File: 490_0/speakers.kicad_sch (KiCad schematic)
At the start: 9 parts, among them J15 Conn_01x07, J16 Conn_01x10, J20 S2B-XH-A, U9 MAX98357A

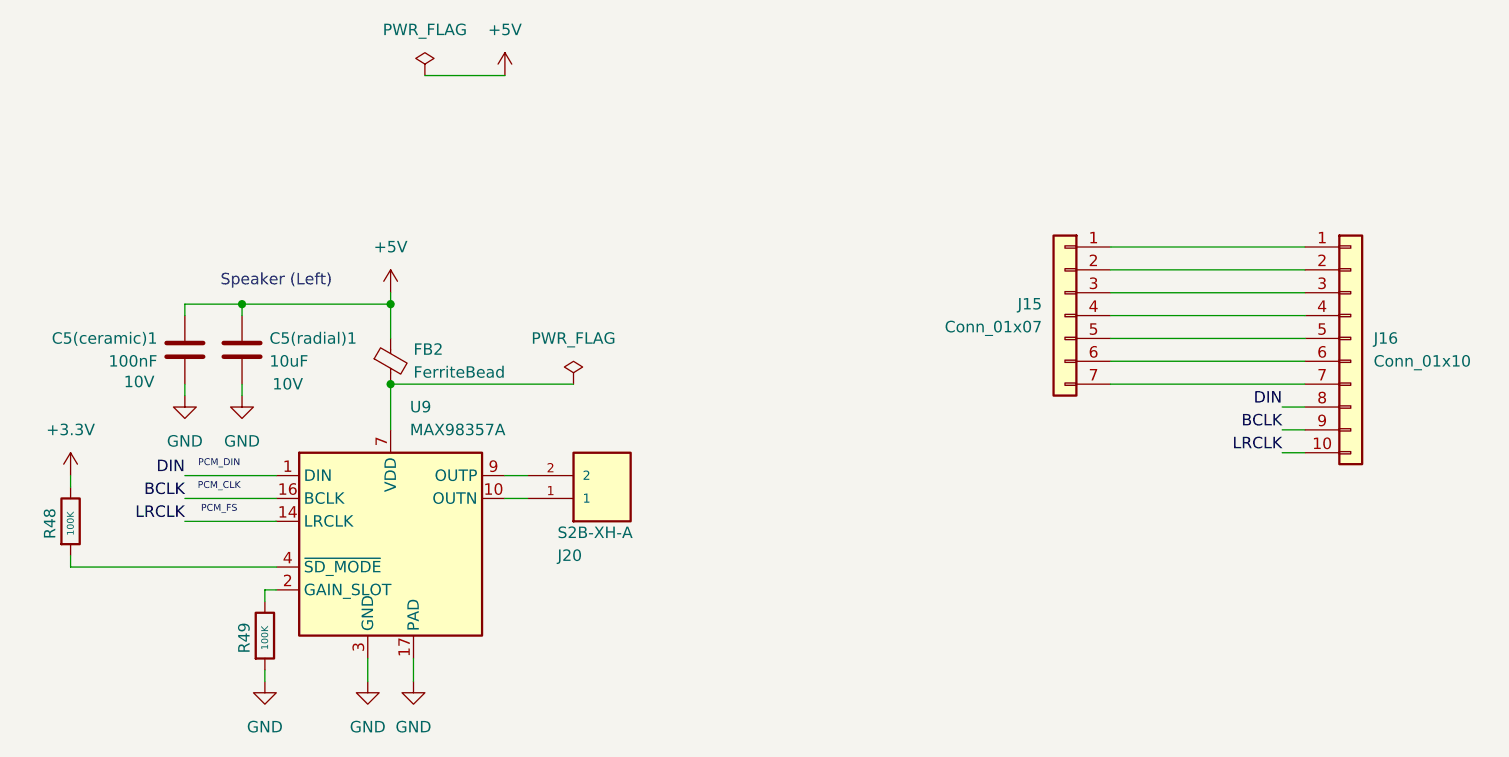
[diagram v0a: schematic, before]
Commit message: Schematic layout update
- applied hierarchical labels
- cleaned up the schematic
- finalized CM4 connections
- checked cm4 connections
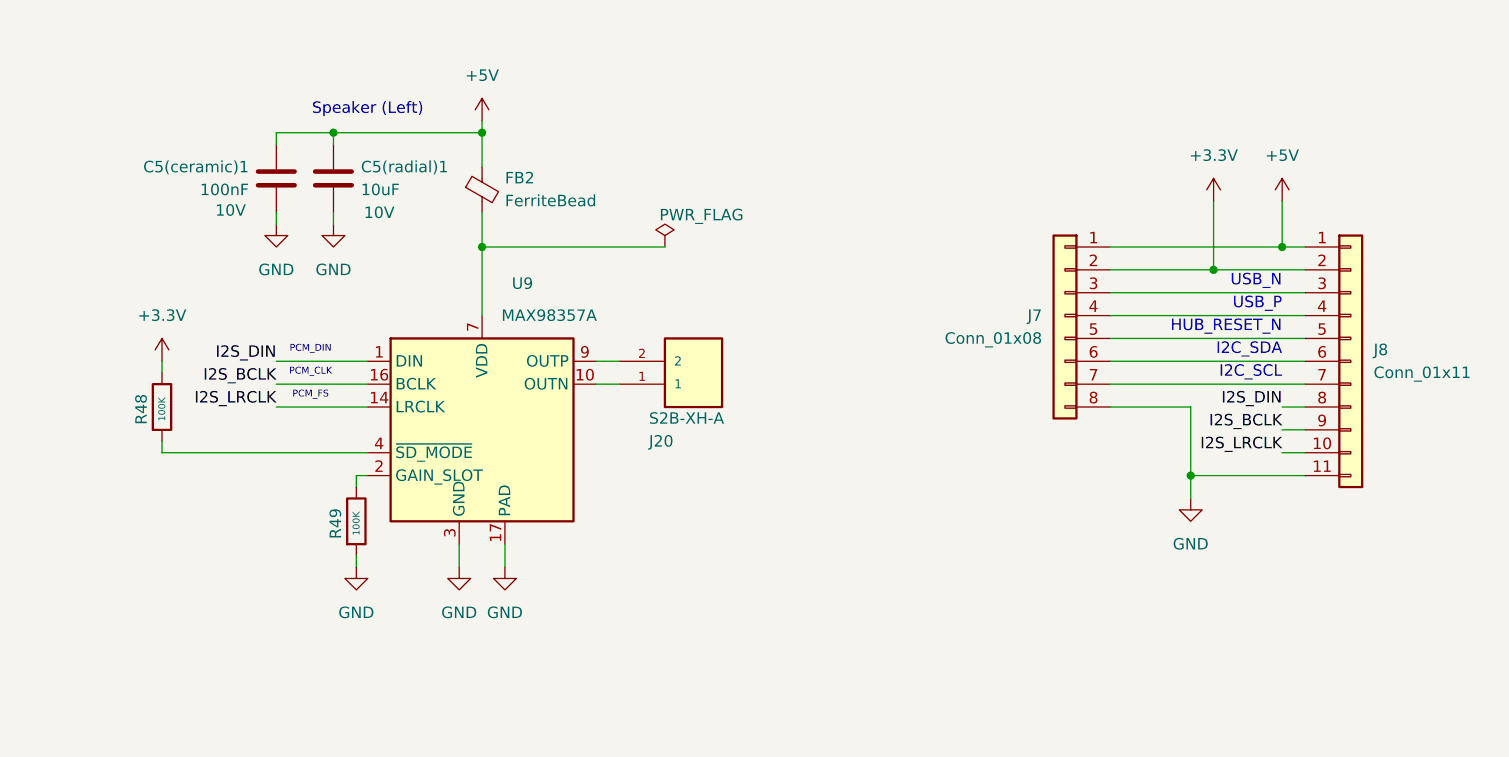
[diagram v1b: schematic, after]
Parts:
- removed J15: Conn_01x07, symbol Connector_Generic:Conn_01x07
- removed J16: Conn_01x10, symbol Connector_Generic:Conn_01x10
- added J7: Conn_01x08, 4ms_Connector:Pins_1x08_2.54mm_TH, symbol PCM_4ms_Connector:Conn_01x08
- added J8: Conn_01x11, symbol Connector_Generic:Conn_01x11
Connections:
- net +3.3V: now also J7.2 (Pin_2), J8.2 (Pin_2)
- net +5V: now also J7.1 (Pin_1), J8.1 (Pin_1)
- net GND: now also J7.8 (Pin_8), J8.11 (Pin_11)
- net BCLK renamed I2S_BCLK
- net I2S_BCLK: now also J8.9 (Pin_9)
- net DIN renamed I2S_DIN
- net I2S_DIN: now also J8.8 (Pin_8)
- net LRCLK renamed I2S_LRCLK
- net I2S_LRCLK: now also J8.10 (Pin_10)
- new net: J7.3 (Pin_3), J8.3 (Pin_3)
- new net: J7.4 (Pin_4), J8.4 (Pin_4)
- new net: J7.5 (Pin_5), J8.5 (Pin_5)
- new net: J7.6 (Pin_6), J8.6 (Pin_6)
- new net: J7.7 (Pin_7), J8.7 (Pin_7)
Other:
- note added: "HUB_RESET_N"
- note added: "I2C_SCL"
- note added: "I2C_SDA"
- note added: "USB_N"
- note added: "USB_P"
- moved on the sheet: C5(ceramic)1, C5(radial)1, FB2, J20, R48, R49, U9

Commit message: Power + BOM update
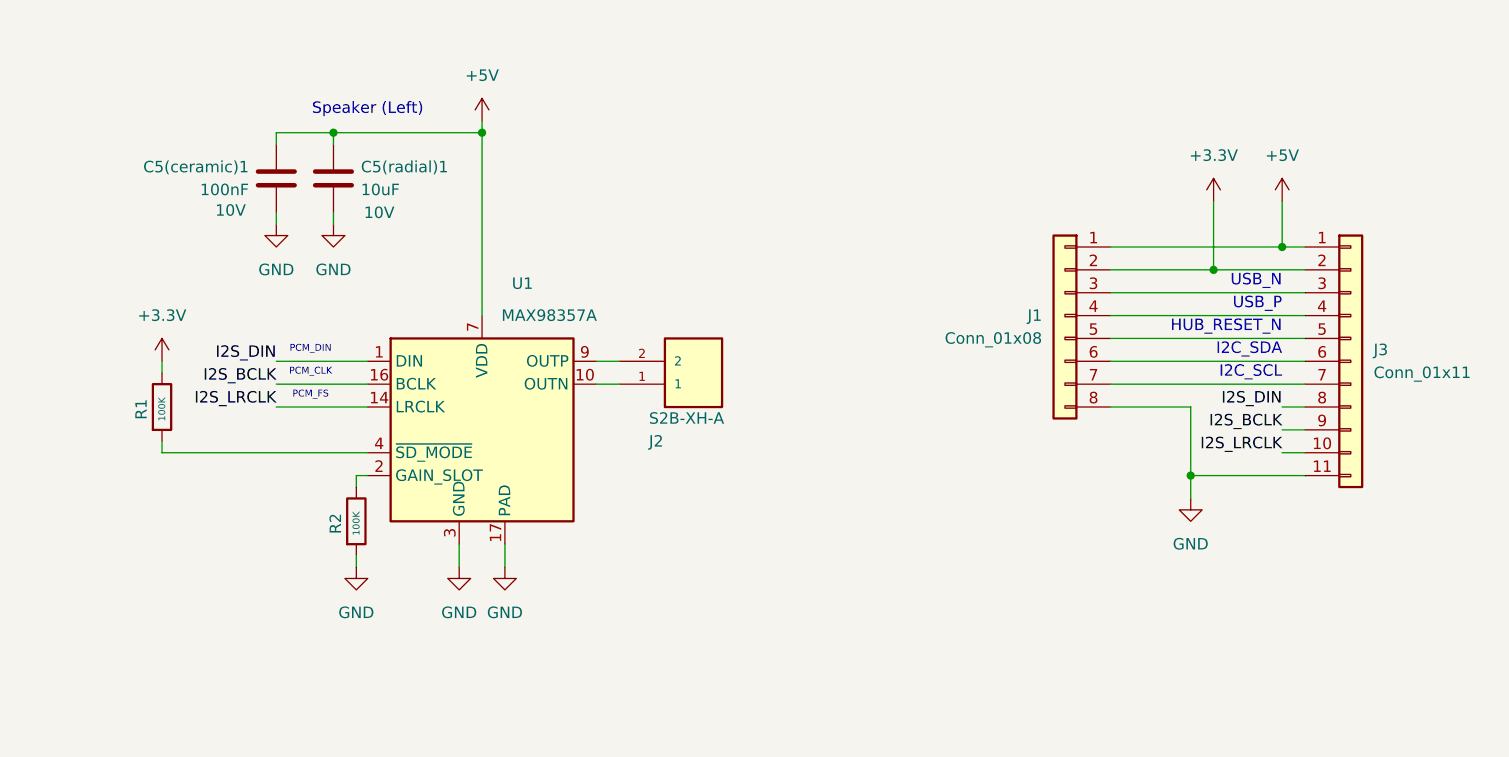
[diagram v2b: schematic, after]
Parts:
- removed FB2: FerriteBead, Capacitor_SMD:C_0603_1608Metric, symbol Device:FerriteBead_Small
- renumbered J7 to J1, J20 to J2, J8 to J3, R48 to R1, R49 to R2, U9 to U1
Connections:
- net +5V: now also U1.7 (VDD), U1.8 (VDD)

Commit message: finished BOM
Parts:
- removed C5(ceramic)1: 100nF, Capacitor_SMD:C_0603_1608Metric, symbol Device:C
- removed C5(radial)1: 10uF, Capacitor_THT:CP_Radial_D5.0mm_P2.50mm, symbol Device:C
- added C52: 100n, symbol Device:C
- added C53: 10u, symbol Device:C
- J1: footprint 4ms_Connector:Pins_1x08_2.54mm_TH -> (none); Digikey Link (none) -> https://www.digikey.ca/en/products/detail/jst-sales-america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; Manufacturer (none) -> JST Sales America Inc.; Manufacturer Part (none) -> S8B-XH-A; Price (none) -> 0.33; Supplier (none) -> DigiKey; Supplier P/N (none) -> 455-S8B-XH-A-ND; Type (none) -> Through Hole; Unit (none) -> pcs
- J3: Digikey Link (none) -> https://www.digikey.ca/en/products/detail/jst-sales-america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; Manufacturer (none) -> JST Sales America Inc.; Manufacturer Part (none) -> S11B-XH-A; Price (none) -> 0.47; Supplier (none) -> DigiKey; Supplier P/N (none) -> 455-S11B-XH-A-ND; Type (none) -> Through Hole; Unit (none) -> pcs
- R1, R2: Digikey Link (none) -> https://www.digikey.ca/en/products/detail/yageo/RC1206FR-07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; Manufacturer (none) -> YAGEO; Manufacturer Part (none) -> RC1206FR-07100KL; Package (none) -> 1206; Price (none) -> 0.1; Supplier (none) -> DigiKey; Supplier P/N (none) -> 311-100KFRCT-ND; Type (none) -> SMD; Unit (none) -> pcs
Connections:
- net +5V: now also C52.1, C53.1
- net GND: now also C52.2, C53.2
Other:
- note added: "10V"

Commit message: Updated the schematic
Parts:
- removed J1: Conn_01x08, symbol PCM_4ms_Connector:Conn_01x08
- removed J3: Conn_01x11, symbol Connector_Generic:Conn_01x11
- renumbered C52 to C35, C53 to C36, J2 to J25, R1 to R37, R2 to R38, U1 to U7
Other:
- note removed: "HUB_RESET_N"
- note removed: "I2C_SCL"
- note removed: "I2C_SDA"
- note removed: "USB_N"
- note removed: "USB_P"
- moved on the sheet: R37

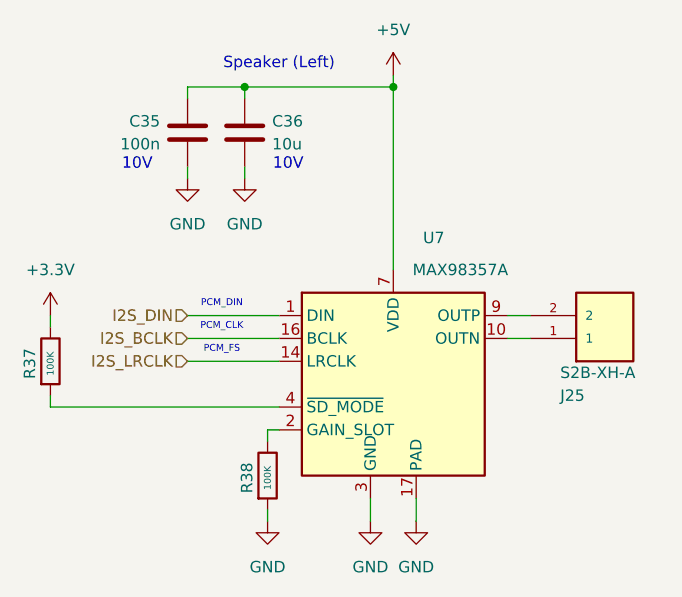
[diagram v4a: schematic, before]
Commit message: Implemented Dmitry comments
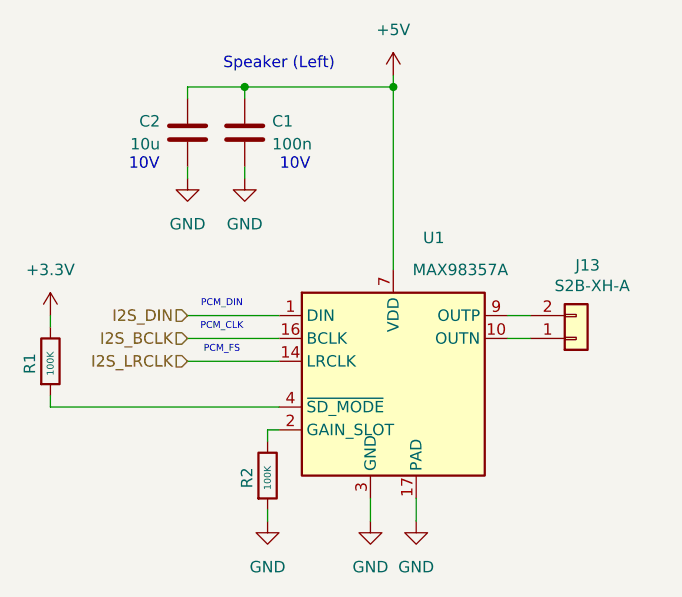
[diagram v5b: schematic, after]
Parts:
- removed J25: S2B-XH-A, S2B-XH-A:JST_S2B-XH-A, symbol capstone_parts:S2B-XH-A
- added J13: S2B-XH-A, S2B-XH-A:JST_S2B-XH-A, symbol PCM_4ms_Connector:Conn_01x02
- renumbered C35 to C1, C36 to C2, R37 to R1, R38 to R2, U7 to U1
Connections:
- net at U1.10 (OUTN): now also J13.1 (Pin_1)
- net at U1.9 (OUTP): now also J13.2 (Pin_2)
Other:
- moved on the sheet: C1, C2

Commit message: Final Fixes
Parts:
- renumbered C2 to C1, C1 to C2, J13 to J1
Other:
- note added: "16V"
- note removed: "10V"
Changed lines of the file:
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@@
 		)
 	)
-	(text "10V"
+	(text "16V"
 		(exclude_from_sim no)
 		(at 96.774 69.596 0)
@@
 		)
 	)
-	(text "10V"
+	(text "16V"
 		(exclude_from_sim no)
 		(at 113.538 69.596 0)
@@
 		(on_board yes)
 		(dnp no)
-		(property "Reference" "J13"
+		(property "Reference" "J1"
 			(at 146.05 80.772 0)
 			(effects
@@
 			(project "490_0"
 				(path "/365a82ed-827d-43e1-aa2f-b98221c4179c/f9f22bb2-829e-4ff5-89be-c4b5e2122135/53573971-fb61-48df-903f-f9c3fbfa6843"
-					(reference "J13")
+					(reference "J1")
 					(unit 1)
 				)
@@
 		(on_board yes)
 		(dnp no)
-		(property "Reference" "C1"
+		(property "Reference" "C2"
 			(at 110.998 64.77 0)
 			(effects
@@
 			(project "490_0"
 				(path "/365a82ed-827d-43e1-aa2f-b98221c4179c/f9f22bb2-829e-4ff5-89be-c4b5e2122135/53573971-fb61-48df-903f-f9c3fbfa6843"
-					(reference "C1")
+					(reference "C2")
 					(unit 1)
 				)
@@
 		(dnp no)
 		(fields_autoplaced yes)
-		(property "Reference" "#PWR03"
+		(property "Reference" "#PWR02"
 			(at 101.6 77.47 0)
 			(effects
@@
 			(project "490_0"
 				(path "/365a82ed-827d-43e1-aa2f-b98221c4179c/f9f22bb2-829e-4ff5-89be-c4b5e2122135/53573971-fb61-48df-903f-f9c3fbfa6843"
-					(reference "#PWR03")
+					(reference "#PWR02")
 					(unit 1)
 				)
@@
 		(dnp no)
 		(fields_autoplaced yes)
-		(property "Reference" "#PWR02"
+		(property "Reference" "#PWR03"
 			(at 107.95 77.47 0)
 			(effects
@@
 			(project "490_0"
 				(path "/365a82ed-827d-43e1-aa2f-b98221c4179c/f9f22bb2-829e-4ff5-89be-c4b5e2122135/53573971-fb61-48df-903f-f9c3fbfa6843"
-					(reference "#PWR02")
+					(reference "#PWR03")
 					(unit 1)
 				)
@@
 		(on_board yes)
 		(dnp no)
-		(property "Reference" "C2"
+		(property "Reference" "C1"
 			(at 98.552 64.77 0)
 			(effects
@@
 			(project "490_0"
 				(path "/365a82ed-827d-43e1-aa2f-b98221c4179c/f9f22bb2-829e-4ff5-89be-c4b5e2122135/53573971-fb61-48df-903f-f9c3fbfa6843"
-					(reference "C2")
+					(reference "C1")
 					(unit 1)
 				)

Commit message: update
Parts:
- J1: now not fitted; now left out of the parts list
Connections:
- net +5V is gone; now on net +3.3V: C1.1, C2.1, U1.7 (VDD), U1.8 (VDD)
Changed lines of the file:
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@@
 			)
 		)
-		(property "Value" "+5V"
+		(property "Value" "+3.3V"
 			(at 124.46 54.61 0)
 			(effects
@@
 		(unit 1)
 		(exclude_from_sim no)
-		(in_bom yes)
+		(in_bom no)
 		(on_board yes)
-		(dnp no)
+		(dnp yes)
 		(property "Reference" "J1"
 			(at 146.05 80.772 0)

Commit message: Implemented Dmitry recommendations
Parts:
- J1: now fitted
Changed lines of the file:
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@@
 		(in_bom no)
 		(on_board yes)
-		(dnp yes)
+		(dnp no)
 		(property "Reference" "J1"
 			(at 146.05 80.772 0)
